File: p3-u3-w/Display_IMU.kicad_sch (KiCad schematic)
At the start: 1 part, among them J2 SWD_pin

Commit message: added in power side and mostly finished schematics :)
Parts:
- added C13, C14: 100nF, symbol Device:C
- added J5: UART, symbol Connector:Conn_01x02_Pin
- added R1: 1k, symbol Device:R
- added R17, R18, R19, R2, R20, R21: 10k, symbol Device:R
- added SW1, SW3, SW4, SW5, SW6, SW7: SW_SPST, symbol Switch:SW_SPST
- added U1: LSM6DSM, Package_LGA:LGA-14_3x2.5mm_P0.5mm_LayoutBorder3x4y, symbol Sensor_Motion:LSM6DSM
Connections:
- net +3V3: now also C13.2, C14.2, R1.1, SW1.2 (B), SW3.2 (B), SW4.2 (B), SW5.2 (B), SW6.2 (B), SW7.2 (B), U1.5 (VDDIO), U1.8 (VDD)
- net GND: now also C13.1, C14.1, R17.1, R18.1, R19.1, R2.1, R20.1, R21.1, U1.6 (GND), U1.7 (GND)
- net I2C_SDA: now also U1.14 (SDA)
- net I2S_SCK: now also U1.13 (SCL)
- new net: R1.2, U1.12 (CS)
- new net BTN_MENU: R19.2, SW5.1 (A)
- new net BTN_NEXT: R18.2, SW4.1 (A)
- new net BTN_PLY: R2.2, SW1.1 (A)
- new net BTN_PREV: R17.2, SW3.1 (A)
- new net BTN_VOL+: R20.2, SW6.1 (A)
- new net BTN_VOL-: R21.2, SW7.1 (A)
- new net IMU_INT1: U1.4 (INT1)
- new net IMU_INT2: U1.9 (INT2)
- new net IMU_SAO: U1.1 (SDO/SA0)
- new net UART_RX: J5.2 (Pin_2)
- new net UART_TX: J5.1 (Pin_1)
- no-connect marks 0 -> 4
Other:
- moved on the sheet: J2

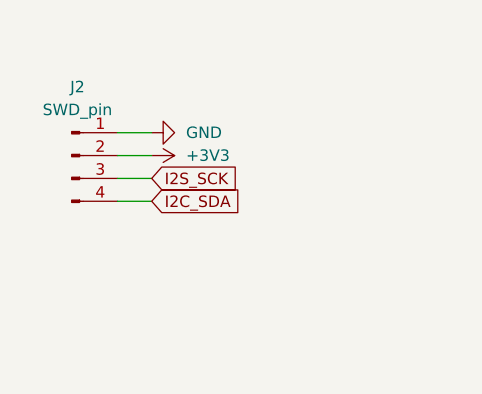
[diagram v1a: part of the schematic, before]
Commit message: finished schematics, started routing and layout.
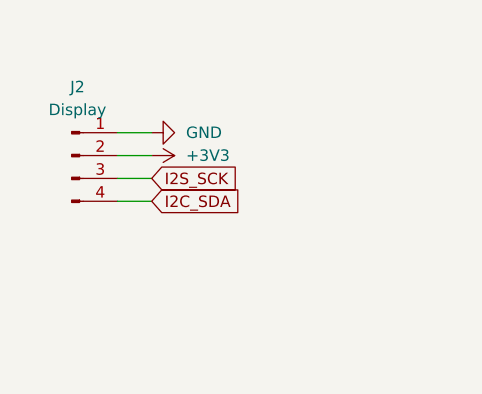
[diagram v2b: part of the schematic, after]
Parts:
- C13, C14: footprint (none) -> Capacitor_SMD:C_0603_1608Metric
- J2: value SWD_pin -> Display; footprint (none) -> Connector_PinHeader_2.54mm:PinHeader_1x04_P2.54mm_Vertical
- J5: footprint (none) -> Connector_PinHeader_1.00mm:PinHeader_1x02_P1.00mm_Vertical
- R1, R17, R18, R19, R2, R20, R21: footprint (none) -> Resistor_SMD:R_0603_1608Metric
- SW1, SW3, SW4, SW5, SW6, SW7: footprint (none) -> Button_Switch_SMD:Panasonic_EVQPUL_EVQPUC
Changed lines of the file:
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@@
 			)
 		)
-		(property "Footprint" ""
+		(property "Footprint" "Resistor_SMD:R_0603_1608Metric"
 			(at 63.5 115.062 90)
 			(effects
@@
 			)
 		)
-		(property "Footprint" ""
+		(property "Footprint" "Capacitor_SMD:C_0603_1608Metric"
 			(at 167.3352 63.5 0)
 			(effects
@@
 			)
 		)
-		(property "Footprint" ""
+		(property "Footprint" "Button_Switch_SMD:Panasonic_EVQPUL_EVQPUC"
 			(at 63.5 124.46 0)
 			(effects
@@
 			)
 		)
-		(property "Footprint" ""
+		(property "Footprint" "Resistor_SMD:R_0603_1608Metric"
 			(at 63.5 174.752 90)
 			(effects
@@
 			)
 		)
-		(property "Footprint" ""
+		(property "Footprint" "Button_Switch_SMD:Panasonic_EVQPUL_EVQPUC"
 			(at 63.5 110.49 0)
 			(effects
@@
 			)
 		)
-		(property "Footprint" ""
+		(property "Footprint" "Resistor_SMD:R_0603_1608Metric"
 			(at 63.5 129.032 90)
 			(effects
@@
 			)
 		)
-		(property "Footprint" ""
+		(property "Footprint" "Button_Switch_SMD:Panasonic_EVQPUL_EVQPUC"
 			(at 63.5 154.94 0)
 			(effects
@@
 			)
 		)
-		(property "Footprint" ""
+		(property "Footprint" "Resistor_SMD:R_0603_1608Metric"
 			(at 63.5 101.092 90)
 			(effects
@@
 			)
 		)
-		(property "Footprint" ""
+		(property "Footprint" "Button_Switch_SMD:Panasonic_EVQPUL_EVQPUC"
 			(at 63.5 96.52 0)
 			(effects
@@
 			)
 		)
-		(property "Value" "SWD_pin"
+		(property "Value" "Display"
 			(at 52.705 31.75 0)
 			(effects
@@
 			)
 		)
-		(property "Footprint" ""
+		(property "Footprint" "Connector_PinHeader_2.54mm:PinHeader_1x04_P2.54mm_Vertical"
 			(at 52.07 36.83 0)
 			(effects
@@
 			)
 		)
-		(property "Footprint" ""
+		(property "Footprint" "Button_Switch_SMD:Panasonic_EVQPUL_EVQPUC"
 			(at 63.5 139.7 0)
 			(effects
@@
 			)
 		)
-		(property "Footprint" ""
+		(property "Footprint" "Button_Switch_SMD:Panasonic_EVQPUL_EVQPUC"
 			(at 63.5 170.18 0)
 			(effects
@@
 			)
 		)
-		(property "Footprint" ""
+		(property "Footprint" "Resistor_SMD:R_0603_1608Metric"
 			(at 123.952 35.56 90)
 			(effects
@@
 			)
 		)
-		(property "Footprint" ""
+		(property "Footprint" "Resistor_SMD:R_0603_1608Metric"
 			(at 63.5 159.512 90)
 			(effects
@@
 			)
 		)
-		(property "Footprint" ""
+		(property "Footprint" "Connector_PinHeader_1.00mm:PinHeader_1x02_P1.00mm_Vertical"
 			(at 52.07 69.85 0)
 			(effects
@@
 			)
 		)
-		(property "Footprint" ""
+		(property "Footprint" "Capacitor_SMD:C_0603_1608Metric"
 			(at 157.1752 63.5 0)
 			(effects
@@
 			)
 		)
-		(property "Footprint" ""
+		(property "Footprint" "Resistor_SMD:R_0603_1608Metric"
 			(at 63.5 144.272 90)
 			(effects

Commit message: changed some routing
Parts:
- C13, C14: footprint Capacitor_SMD:C_0603_1608Metric -> Capacitor_SMD:C_0402_1005Metric
- R1, R17, R18, R19, R2, R20, R21: footprint Resistor_SMD:R_0603_1608Metric -> Resistor_SMD:R_0402_1005Metric
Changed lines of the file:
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@@
 			)
 		)
-		(property "Footprint" "Resistor_SMD:R_0603_1608Metric"
+		(property "Footprint" "Resistor_SMD:R_0402_1005Metric"
 			(at 63.5 115.062 90)
 			(effects
@@
 			)
 		)
-		(property "Footprint" "Capacitor_SMD:C_0603_1608Metric"
+		(property "Footprint" "Capacitor_SMD:C_0402_1005Metric"
 			(at 167.3352 63.5 0)
 			(effects
@@
 			)
 		)
-		(property "Footprint" "Resistor_SMD:R_0603_1608Metric"
+		(property "Footprint" "Resistor_SMD:R_0402_1005Metric"
 			(at 63.5 174.752 90)
 			(effects
@@
 			)
 		)
-		(property "Footprint" "Resistor_SMD:R_0603_1608Metric"
+		(property "Footprint" "Resistor_SMD:R_0402_1005Metric"
 			(at 63.5 129.032 90)
 			(effects
@@
 			)
 		)
-		(property "Footprint" "Resistor_SMD:R_0603_1608Metric"
+		(property "Footprint" "Resistor_SMD:R_0402_1005Metric"
 			(at 63.5 101.092 90)
 			(effects
@@
 			)
 		)
-		(property "Footprint" "Resistor_SMD:R_0603_1608Metric"
+		(property "Footprint" "Resistor_SMD:R_0402_1005Metric"
 			(at 123.952 35.56 90)
 			(effects
@@
 			)
 		)
-		(property "Footprint" "Resistor_SMD:R_0603_1608Metric"
+		(property "Footprint" "Resistor_SMD:R_0402_1005Metric"
 			(at 63.5 159.512 90)
 			(effects
@@
 			)
 		)
-		(property "Footprint" "Capacitor_SMD:C_0603_1608Metric"
+		(property "Footprint" "Capacitor_SMD:C_0402_1005Metric"
 			(at 157.1752 63.5 0)
 			(effects
@@
 			)
 		)
-		(property "Footprint" "Resistor_SMD:R_0603_1608Metric"
+		(property "Footprint" "Resistor_SMD:R_0402_1005Metric"
 			(at 63.5 144.272 90)
 			(effects

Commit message: added in some more routing.
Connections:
- net I2S_SCK renamed I2C_SCL
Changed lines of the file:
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@@
+		)
+	)
+	(global_label "I2C_SCL"
+		(shape input)
+		(at 128.27 39.37 90)
+		(fields_autoplaced yes)
+		(effects
+			(font
+				(size 1.27 1.27)
+			)
+			(justify left)
+		)
+		(property "Intersheetrefs" "${INTERSHEET_REFS}"
+			(at 128.27 28.8253 90)
+			(effects
+				(font
+					(size 1.27 1.27)
+				)
+				(justify left)
+				(hide yes)
+			)
 		)
 	)
@@
 		)
 	)
+	(global_label "I2C_SCL"
+		(shape input)
+		(at 60.96 39.37 0)
+		(fields_autoplaced yes)
+		(effects
+			(font
+				(size 1.27 1.27)
+			)
+			(justify left)
+		)
+		(property "Intersheetrefs" "${INTERSHEET_REFS}"
+			(at 71.5047 39.37 0)
+			(effects
+				(font
+					(size 1.27 1.27)
+				)
+				(justify left)
+				(hide yes)
+			)
+		)
+	)
 	(global_label "BTN_VOL+"
 		(shape input)
@@
 		)
 	)
-	(global_label "I2S_SCK"
-		(shape input)
-		(at 128.27 39.37 90)
-		(fields_autoplaced yes)
-		(effects
-			(font
-				(size 1.27 1.27)
-			)
-			(justify left)
-		)
-		(property "Intersheetrefs" "${INTERSHEET_REFS}"
-			(at 128.27 28.6439 90)
-			(effects
-				(font
-					(size 1.27 1.27)
-				)
-				(justify left)
-				(hide yes)
-			)
-		)
-	)
 	(global_label "IMU_SAO"
 		(shape input)
@@
 			(effects
 				(font
-					(size 1.27 1.27)
-				)
-				(justify left)
-				(hide yes)
-			)
-		)
-	)
-	(global_label "I2S_SCK"
-		(shape input)
-		(at 60.96 39.37 0)
-		(fields_autoplaced yes)
-		(effects
-			(font
-				(size 1.27 1.27)
-			)
-			(justify left)
-		)
-		(property "Intersheetrefs" "${INTERSHEET_REFS}"
-			(at 71.6861 39.37 0)
-			(effects
-				(font

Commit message: finished the pcb, added in BOM
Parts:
- removed J5: UART, Connector_PinHeader_1.00mm:PinHeader_1x02_P1.00mm_Vertical, symbol Connector:Conn_01x02_Pin
